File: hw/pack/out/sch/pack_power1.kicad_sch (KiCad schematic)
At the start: 20 parts, among them Q1 DMG2305UX, SW1 recessed slide, U4 TPS61023, U5 TLV75533P, U6 TLV75533P

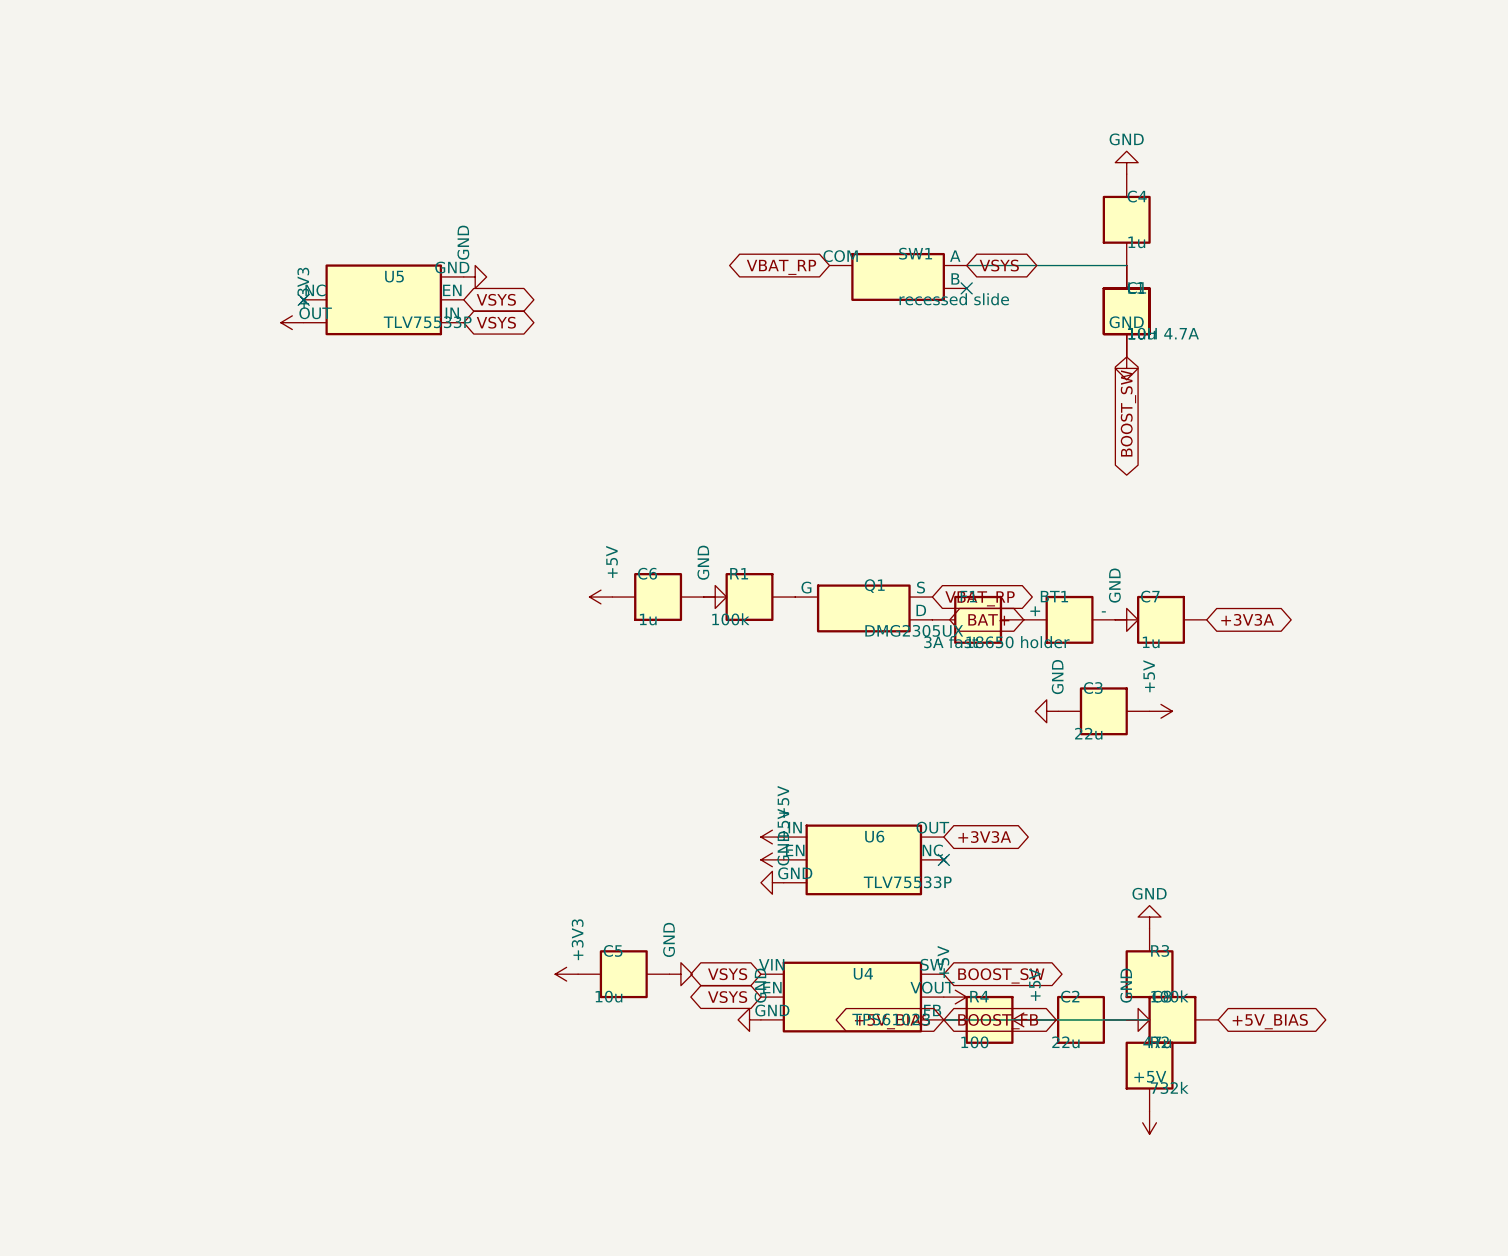
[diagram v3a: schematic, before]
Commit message: hw/pack: 4-layer pack PCB layout, review fixes, fab outputs, cost-down (#104)
* hw/pack: scripted 4-layer layout from the netlist, DRC clean (#34)

layout.py builds pack.kicad_pcb from out/pack.net with pcbnew: outline from
mech/pack.py, BT40NE antenna past the board edge, TI-pattern boost cell,
grid maze router (router.py), GND fan-out vias, RF via fence, JLC rules in
pack.kicad_dru. outputs.py writes gerbers/drill/BOM/CPL/STEP and renders.

Co-Authored-By: Claude Opus 5.5 <noreply@anthropic.com>

* hw/pack: enclosure fit (fit.py + CadQuery test), mech outline from the layout, layout tests (#34)

mech/pack.py takes the real outline (73.4 x 35 mm, post notch), z0 +1.4 mm so
the module antenna clears the clip bosses, and the antenna overhang as a part.
fit.py checks board/parts/openings/lid features without CadQuery and renders
fit_top/fit_side.png; tests/mech/test_pack_fit.py does it with the STEP.
tests/test_pack_layout.py: DRC 0 errors, fab outputs fresh, netlist parity.

Co-Authored-By: Claude Opus 5.5 <noreply@anthropic.com>

* hw/REVIEW.md: pack board layout review, fixes and open items (#34)

Co-Authored-By: Claude Opus 5.5 <noreply@anthropic.com>

* hw/pack, mech: SJ1-3543 from datasheet, M2 board retention, light pipes, switch fork, CI pcb job (#34)

- SJ1-3543 footprint from Same Sky SJ1-354X (09/2024): 12x11.6x9.6 body, M6
  bushing through the wall from the inner face, axis 5.2 mm, anchors on GND
- H1/H2 M2 holes + printed pilot bosses (mech PCB_SCREWS), two rests
- lid light-pipe chimneys (lid prints outer-face-down), printed switch fork
  straddling SW1's right-angle actuator through a relocated slot
- mech comps() now the per-part envelope from the layout
- fit.py checks fork, chimneys, screws; CadQuery fit test mandatory under CI
- ci.yml: pcb job (KiCad 10 PPA) runs tests/test_pack_layout.py
- REVIEW: holder BH-18650-W and pigtail Molex 0731160017 chosen; with them
  PK-12 would be ~$38.2 > $35, prices.py left unchanged pending decision

Co-Authored-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
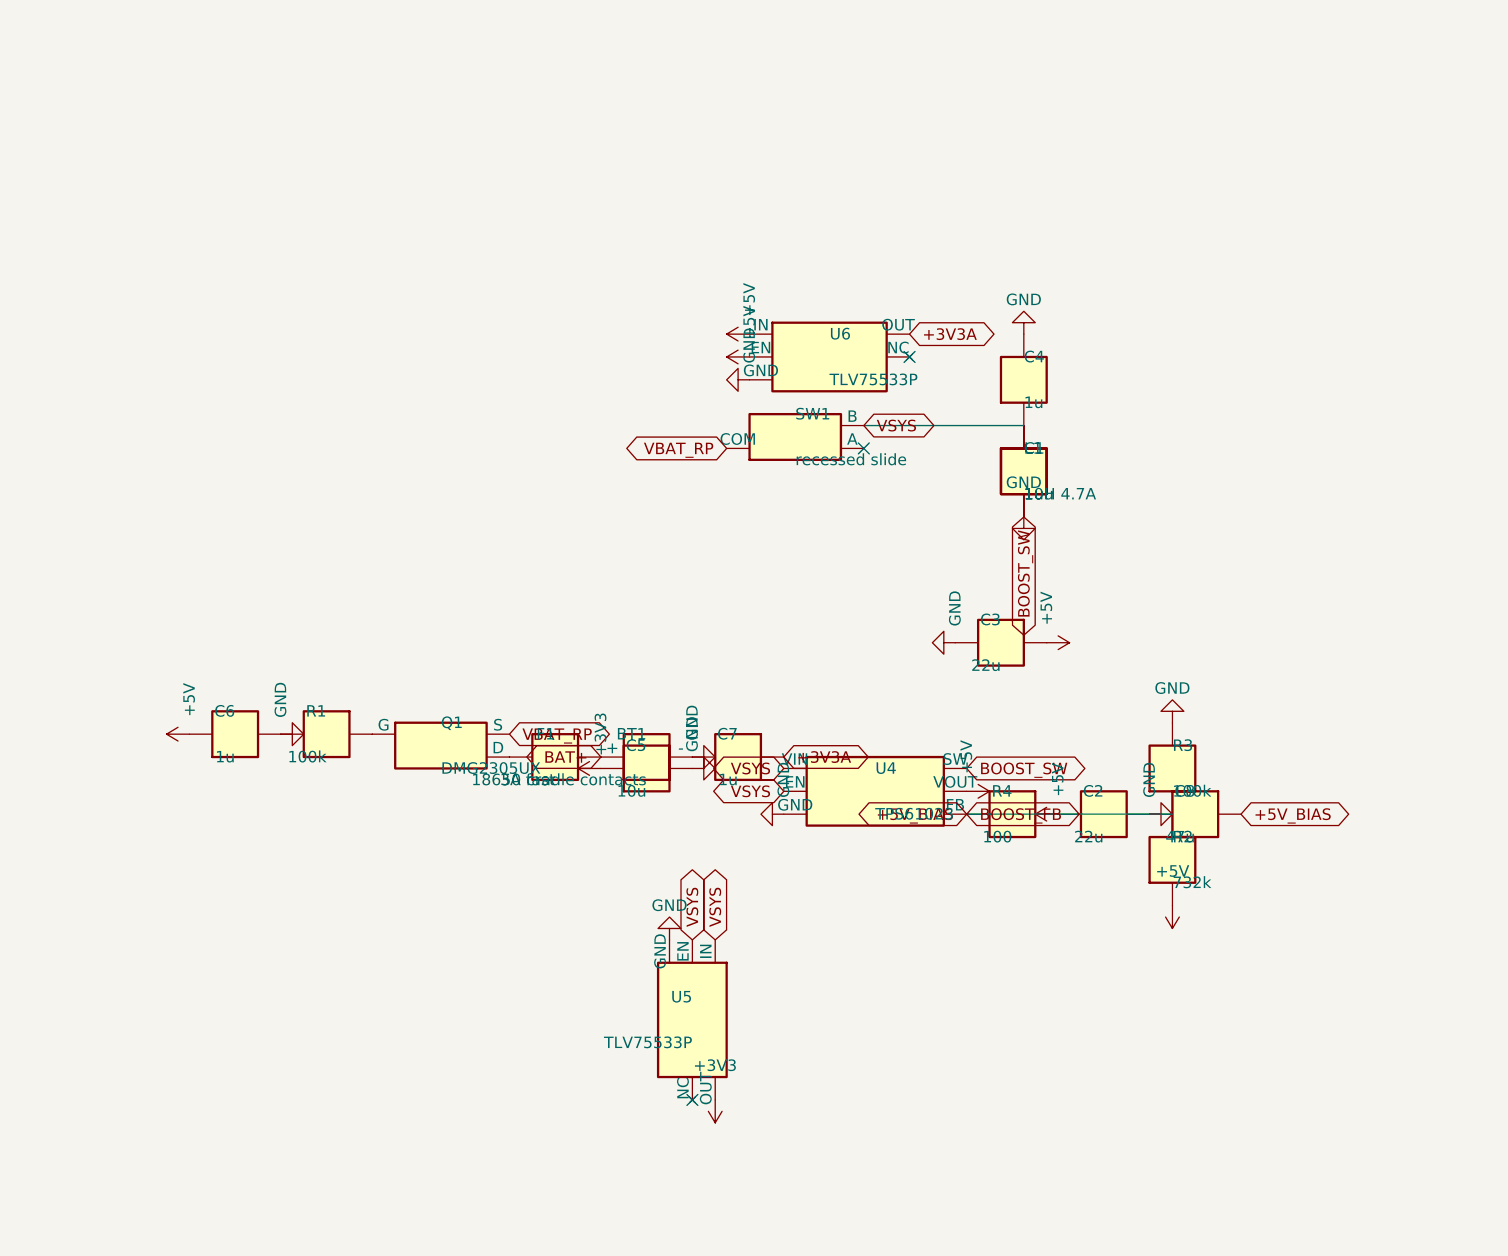
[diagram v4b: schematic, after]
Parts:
- BT1: value 18650 holder -> 18650 cradle contacts; footprint openpack:BH-18650-B1BA002 -> openpack:Cell_Wire_Pads; MPN BH-18650-B1BA002 -> MY-18650-04-J/05-J
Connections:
- net VSYS: now also SW1.3 (B); no longer SW1.1 (A)
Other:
- moved on the sheet: BT1, C1, C2, C3, C4, C5, C6, C7, C8, F1, L1, Q1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
